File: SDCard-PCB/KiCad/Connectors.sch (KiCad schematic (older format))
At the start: 6 parts, among them J22 Conn_01x01, J23 Conn_01x01, J24 Conn_01x01, J25 Conn_01x01, J26 Conn_01x01, J27 Conn_01x01

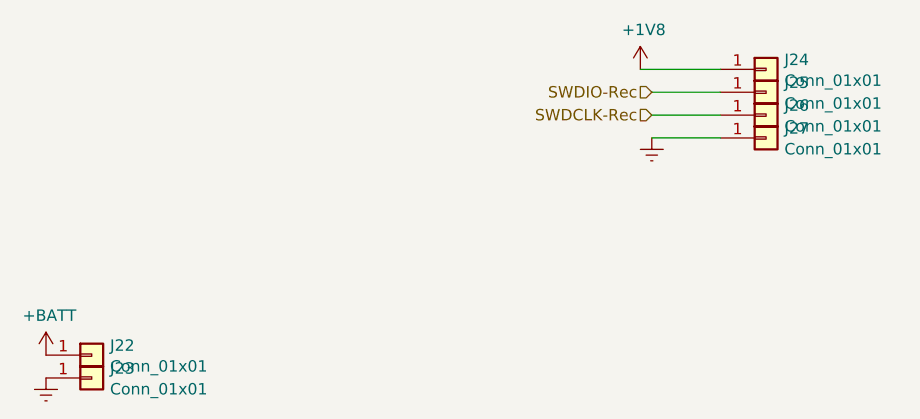
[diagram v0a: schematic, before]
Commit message: Finish schematics, begin PCB design
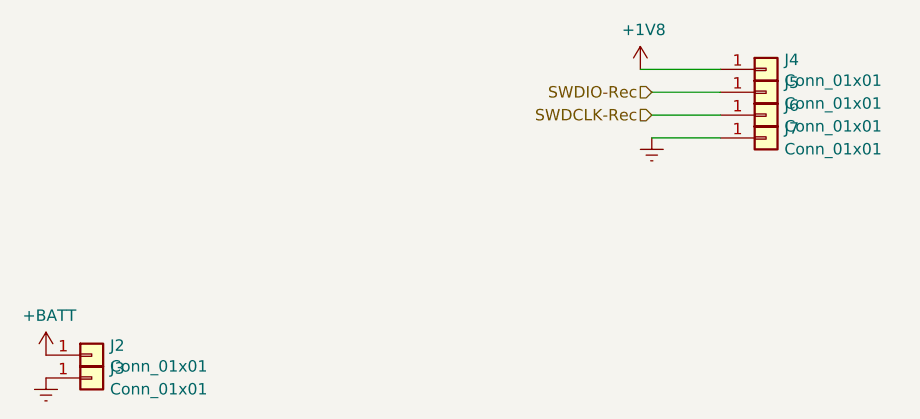
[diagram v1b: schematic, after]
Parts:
- J2: renamed from J22; footprint .Connector:Conn_1x1_250x750_Pad -> Connector_PinHeader_2.54mm:PinHeader_1x01_P2.54mm_Vertical
- J3: renamed from J23; footprint .Connector:Conn_1x1_250x750_Pad -> Connector_PinHeader_2.54mm:PinHeader_1x01_P2.54mm_Vertical
- J4: renamed from J24; footprint .Connector:Conn_1x1_250x750_Pad -> Connector_PinHeader_2.54mm:PinHeader_1x01_P2.54mm_Vertical
- J5: renamed from J25; footprint .Connector:Conn_1x1_250x750_Pad -> Connector_PinHeader_2.54mm:PinHeader_1x01_P2.54mm_Vertical
- J6: renamed from J26; footprint .Connector:Conn_1x1_250x750_Pad -> Connector_PinHeader_2.54mm:PinHeader_1x01_P2.54mm_Vertical
- J7: renamed from J27; footprint .Connector:Conn_1x1_250x750_Pad -> Connector_PinHeader_2.54mm:PinHeader_1x01_P2.54mm_Vertical
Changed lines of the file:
@@
 $Descr A4 11693 8268
 encoding utf-8
-Sheet 4 6
+Sheet 3 6
 Title ""
 Date ""
@@
 $EndDescr
 $Comp
-L .Connector:Conn_01x01 J22
+L .Connector:Conn_01x01 J2
 U 1 1 5CA26767
 P 4450 4100
-F 0 "J22" H 4530 4142 50  0000 L CNN
+F 0 "J2" H 4530 4142 50  0000 L CNN
 F 1 "Conn_01x01" H 4530 4051 50  0000 L CNN
-F 2 ".Connector:Conn_1x1_250x750_Pad" H 4450 4100 50  0001 C CNN
+F 2 "Connector_PinHeader_2.54mm:PinHeader_1x01_P2.54mm_Vertical" H 4450 4100 50  0001 C CNN
 F 3 "~" H 4450 4100 50  0001 C CNN
 	1    4450 4100
@@
 $EndComp
 $Comp
-L .Connector:Conn_01x01 J23
+L .Connector:Conn_01x01 J3
 U 1 1 5CA267B7
 P 4450 4200
-F 0 "J23" H 4530 4242 50  0000 L CNN
+F 0 "J3" H 4530 4242 50  0000 L CNN
 F 1 "Conn_01x01" H 4530 4151 50  0000 L CNN
-F 2 ".Connector:Conn_1x1_250x750_Pad" H 4450 4200 50  0001 C CNN
+F 2 "Connector_PinHeader_2.54mm:PinHeader_1x01_P2.54mm_Vertical" H 4450 4200 50  0001 C CNN
 F 3 "~" H 4450 4200 50  0001 C CNN
 	1    4450 4200
@@
 $EndComp
 $Comp
-L power:+BATT #PWR047
+L power:+BATT #PWR032
 U 1 1 5CA268F4
 P 4250 4100
-F 0 "#PWR047" H 4250 3950 50  0001 C CNN
+F 0 "#PWR032" H 4250 3950 50  0001 C CNN
 F 1 "+BATT" H 4265 4273 50  0000 C CNN
 F 2 "" H 4250 4100 50  0001 C CNN
@@
 $EndComp
 $Comp
-L power:Earth #PWR048
+L power:Earth #PWR033
 U 1 1 5CA26FF1
 P 4250 4200
-F 0 "#PWR048" H 4250 3950 50  0001 C CNN
+F 0 "#PWR033" H 4250 3950 50  0001 C CNN
 F 1 "Earth" H 4250 4050 50  0001 C CNN
 F 2 "" H 4250 4200 50  0001 C CNN
@@
 $EndComp
 $Comp
-L power:+1V8 #PWR049
+L power:+1V8 #PWR034
 U 1 1 5CC8E5DF
 P 6850 2850
-F 0 "#PWR049" H 6850 2700 50  0001 C CNN
+F 0 "#PWR034" H 6850 2700 50  0001 C CNN
 F 1 "+1V8" H 6865 3023 50  0000 C CNN
 F 2 "" H 6850 2850 50  0001 C CNN
@@
 $EndComp
 $Comp
-L power:Earth #PWR050
+L power:Earth #PWR035
 U 1 1 5CC8E5E5
 P 6900 3150
-F 0 "#PWR050" H 6900 2900 50  0001 C CNN
+F 0 "#PWR035" H 6900 2900 50  0001 C CNN
 F 1 "Earth" H 6900 3000 50  0001 C CNN
 F 2 "" H 6900 3150 50  0001 C CNN
@@
 $EndComp
 $Comp
-L .Connector:Conn_01x01 J24
+L .Connector:Conn_01x01 J4
 U 1 1 5CC8E5EB
 P 7400 2850
-F 0 "J24" H 7480 2892 50  0000 L CNN
+F 0 "J4" H 7480 2892 50  0000 L CNN
 F 1 "Conn_01x01" H 7480 2801 50  0000 L CNN
-F 2 ".Connector:Conn_1x1_250x750_Pad" H 7400 2850 50  0001 C CNN
+F 2 "Connector_PinHeader_2.54mm:PinHeader_1x01_P2.54mm_Vertical" H 7400 2850 50  0001 C CNN
 F 3 "~" H 7400 2850 50  0001 C CNN
 	1    7400 2850
@@
 $EndComp
 $Comp
-L .Connector:Conn_01x01 J25
+L .Connector:Conn_01x01 J5
 U 1 1 5CC8E5F1
 P 7400 2950
-F 0 "J25" H 7480 2992 50  0000 L CNN
+F 0 "J5" H 7480 2992 50  0000 L CNN
 F 1 "Conn_01x01" H 7480 2901 50  0000 L CNN
-F 2 ".Connector:Conn_1x1_250x750_Pad" H 7400 2950 50  0001 C CNN
+F 2 "Connector_PinHeader_2.54mm:PinHeader_1x01_P2.54mm_Vertical" H 7400 2950 50  0001 C CNN
 F 3 "~" H 7400 2950 50  0001 C CNN
 	1    7400 2950
@@
 $EndComp
 $Comp
-L .Connector:Conn_01x01 J26
+L .Connector:Conn_01x01 J6
 U 1 1 5CC8E5F7
 P 7400 3050
-F 0 "J26" H 7480 3092 50  0000 L CNN
+F 0 "J6" H 7480 3092 50  0000 L CNN
 F 1 "Conn_01x01" H 7480 3001 50  0000 L CNN
-F 2 ".Connector:Conn_1x1_250x750_Pad" H 7400 3050 50  0001 C CNN
+F 2 "Connector_PinHeader_2.54mm:PinHeader_1x01_P2.54mm_Vertical" H 7400 3050 50  0001 C CNN
 F 3 "~" H 7400 3050 50  0001 C CNN
 	1    7400 3050
@@
 $EndComp
 $Comp
-L .Connector:Conn_01x01 J27
+L .Connector:Conn_01x01 J7
 U 1 1 5CC8E5FD
 P 7400 3150
-F 0 "J27" H 7480 3192 50  0000 L CNN
+F 0 "J7" H 7480 3192 50  0000 L CNN
 F 1 "Conn_01x01" H 7480 3101 50  0000 L CNN
-F 2 ".Connector:Conn_1x1_250x750_Pad" H 7400 3150 50  0001 C CNN
+F 2 "Connector_PinHeader_2.54mm:PinHeader_1x01_P2.54mm_Vertical" H 7400 3150 50  0001 C CNN
 F 3 "~" H 7400 3150 50  0001 C CNN
 	1    7400 3150
